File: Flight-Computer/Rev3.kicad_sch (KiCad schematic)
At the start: 6 parts, among them J3 Conn_01x04, J4 Conn_01x04, J5 Conn_01x04, J6 Conn_01x04, U15 SST25VF512A-33-4I-SAE

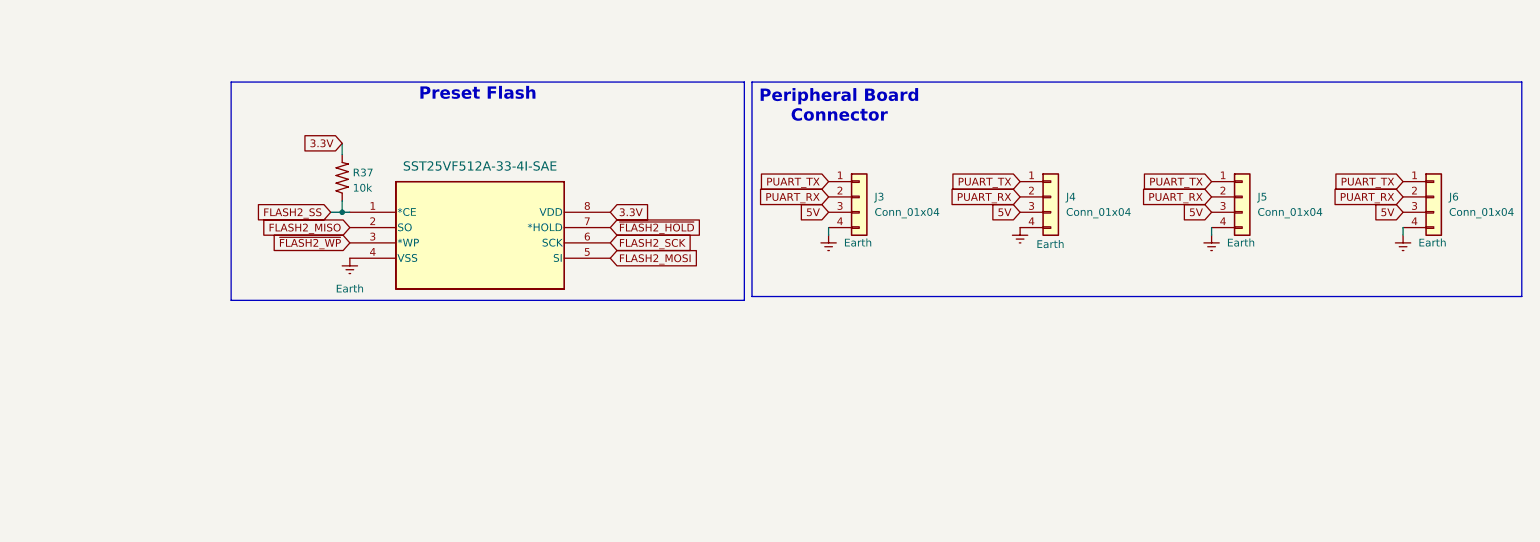
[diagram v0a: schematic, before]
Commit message: SPI Flash Daisy chain
need to review and likely rewire the daisy chain
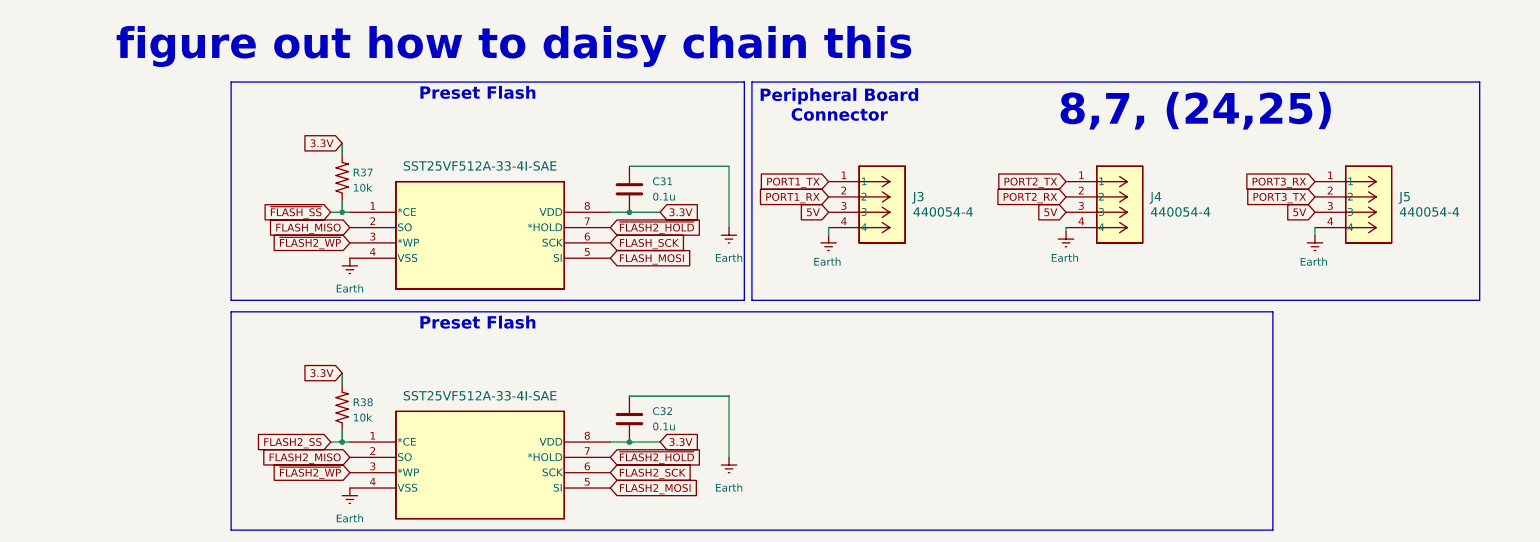
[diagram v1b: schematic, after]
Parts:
- removed J3, J4, J5, J6: Conn_01x04, Connector_JST:JST_PH_B4B-PH-K_1x04_P2.00mm_Vertical, symbol Connector_Generic:Conn_01x04
- added C31, C32: 0.1u, Capacitor_SMD:C_0603_1608Metric, symbol Device:C
- added J3, J4, J5: 440054-4, 440054_4:CONN_440054-4_TEC, symbol 2025-03-27_16-40-08:440054-4
- added R38: 10k, Flight-Computer-Mac:RES_0603, symbol Flight-Computer:RES_0603
- added U14: SST25VF512A-33-4I-SAE, SST25:SOIC8_SA_SST_MCH, symbol SST25VF512A-33-4I-SAE:SST25VF512A-33-4I-SAE
- R37: footprint Flight-Computer:RES_0603 -> Flight-Computer-Mac:RES_0603
- U15: footprint SOIC8_SA_SST_MCH -> SST25:SOIC8_SA_SST_MCH
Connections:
- net 3.3V: now also C31.2, C32.2, R38.2, U14.8 (VDD)
- net 5V: now also J3.3, J4.3, J5.3
- net Earth: now also C31.1, C32.1, J3.4, J4.4, J5.4, U14.4 (VSS)
- net FLASH2_MISO: now also U14.2 (SO); no longer U15.2 (SO)
- net FLASH2_MOSI: now also U14.5 (SI); no longer U15.5 (SI)
- net FLASH2_SCK: now also U14.6 (SCK); no longer U15.6 (SCK)
- net FLASH2_SS: now also R38.1, U14.1 (*CE); no longer R37.1, U15.1 (*CE)
- net ~{FLASH2_HOLD}: now also U14.7 (*HOLD)
- net ~{FLASH2_WP}: now also U14.3 (*WP)
- new net FLASH_MISO: U15.2 (SO)
- new net FLASH_MOSI: U15.5 (SI)
- new net FLASH_SCK: U15.6 (SCK)
- new net PORT1_RX: J3.2
- new net PORT1_TX: J3.1
- new net PORT2_RX: J4.2
- new net PORT2_TX: J4.1
- new net PORT3_RX: J5.1
- new net PORT3_TX: J5.2
- new net ~{FLASH_SS}: R37.1, U15.1 (*CE)
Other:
- note added: "8,7, (24,25)"
- note added: "figure out how to daisy chain this"
